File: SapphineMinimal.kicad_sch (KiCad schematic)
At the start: 0 parts

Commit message: Completed board Rev 1
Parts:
- added FID101, FID102, FID103: Fiducial, Fiducial:Fiducial_0.75mm_Mask2.25mm, symbol Mechanical:Fiducial
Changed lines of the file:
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@@
     (effects (font (size 1.27 1.27)) (justify left bottom))
+  )
+  (symbol (lib_id "Mechanical:Fiducial") (at 255.27 34.29 0) (unit 1)
+    (in_bom yes) (on_board yes) (fields_autoplaced)
+    (property "Reference" "FID102" (id 0) (at 257.429 33.4553 0)
+      (effects (font (size 1.27 1.27)) (justify left))
+    )
+    (property "Value" "Fiducial" (id 1) (at 257.429 35.9922 0)
+      (effects (font (size 1.27 1.27)) (justify left))
+    )
+    (property "Footprint" "Fiducial:Fiducial_0.75mm_Mask2.25mm" (id 2) (at 255.27 34.29 0)
+      (effects (font (size 1.27 1.27)) hide)
+    )
+    (property "Datasheet" "~" (id 3) (at 255.27 34.29 0)
+      (effects (font (size 1.27 1.27)) hide)
+    )
+  )
+  (symbol (lib_id "Mechanical:Fiducial") (at 255.27 25.4 0) (unit 1)
+    (in_bom yes) (on_board yes) (fields_autoplaced)
+    (property "Reference" "FID101" (id 0) (at 257.429 24.5653 0)
+      (effects (font (size 1.27 1.27)) (justify left))
+    )
+    (property "Value" "Fiducial" (id 1) (at 257.429 27.1022 0)
+      (effects (font (size 1.27 1.27)) (justify left))
+    )
+    (property "Footprint" "Fiducial:Fiducial_0.75mm_Mask2.25mm" (id 2) (at 255.27 25.4 0)
+      (effects (font (size 1.27 1.27)) hide)
+    )
+    (property "Datasheet" "~" (id 3) (at 255.27 25.4 0)
+      (effects (font (size 1.27 1.27)) hide)
+    )
+  )
+  (symbol (lib_id "Mechanical:Fiducial") (at 255.27 43.18 0) (unit 1)
+    (in_bom yes) (on_board yes) (fields_autoplaced)
+    (property "Reference" "FID103" (id 0) (at 257.429 42.3453 0)
+      (effects (font (size 1.27 1.27)) (justify left))
+    )
+    (property "Value" "Fiducial" (id 1) (at 257.429 44.8822 0)
+      (effects (font (size 1.27 1.27)) (justify left))
+    )
+    (property "Footprint" "Fiducial:Fiducial_0.75mm_Mask2.25mm" (id 2) (at 255.27 43.18 0)
+      (effects (font (size 1.27 1.27)) hide)
+    )
+    (property "Datasheet" "~" (id 3) (at 255.27 43.18 0)
+      (effects (font (size 1.27 1.27)) hide)
+    )
   )
   (sheet (at 181.61 46.99) (size 38.1 27.94) (fields_autoplaced)
@@
       (reference "FB801") (unit 1) (value "FerriteBead") (footprint "Inductor_SMD:L_0201_0603Metric")
     )
+    (path "/425001ac-1f75-42e4-b850-928c7a40b141"
+      (reference "FID101") (unit 1) (value "Fiducial") (footprint "Fiducial:Fiducial_0.75mm_Mask2.25mm")
+    )
+    (path "/2acc44b4-fb4e-460d-83c5-dc8f7d66c881"
+      (reference "FID102") (unit 1) (value "Fiducial") (footprint "Fiducial:Fiducial_0.75mm_Mask2.25mm")
+    )
+    (path "/ba9cefc2-e855-411c-bf9e-6a189e250684"
+      (reference "FID103") (unit 1) (value "Fiducial") (footprint "Fiducial:Fiducial_0.75mm_Mask2.25mm")
+    )
     (path "/00000000-0000-0000-0000-00005e3fe689/00000000-0000-0000-0000-00005e66dbe9"

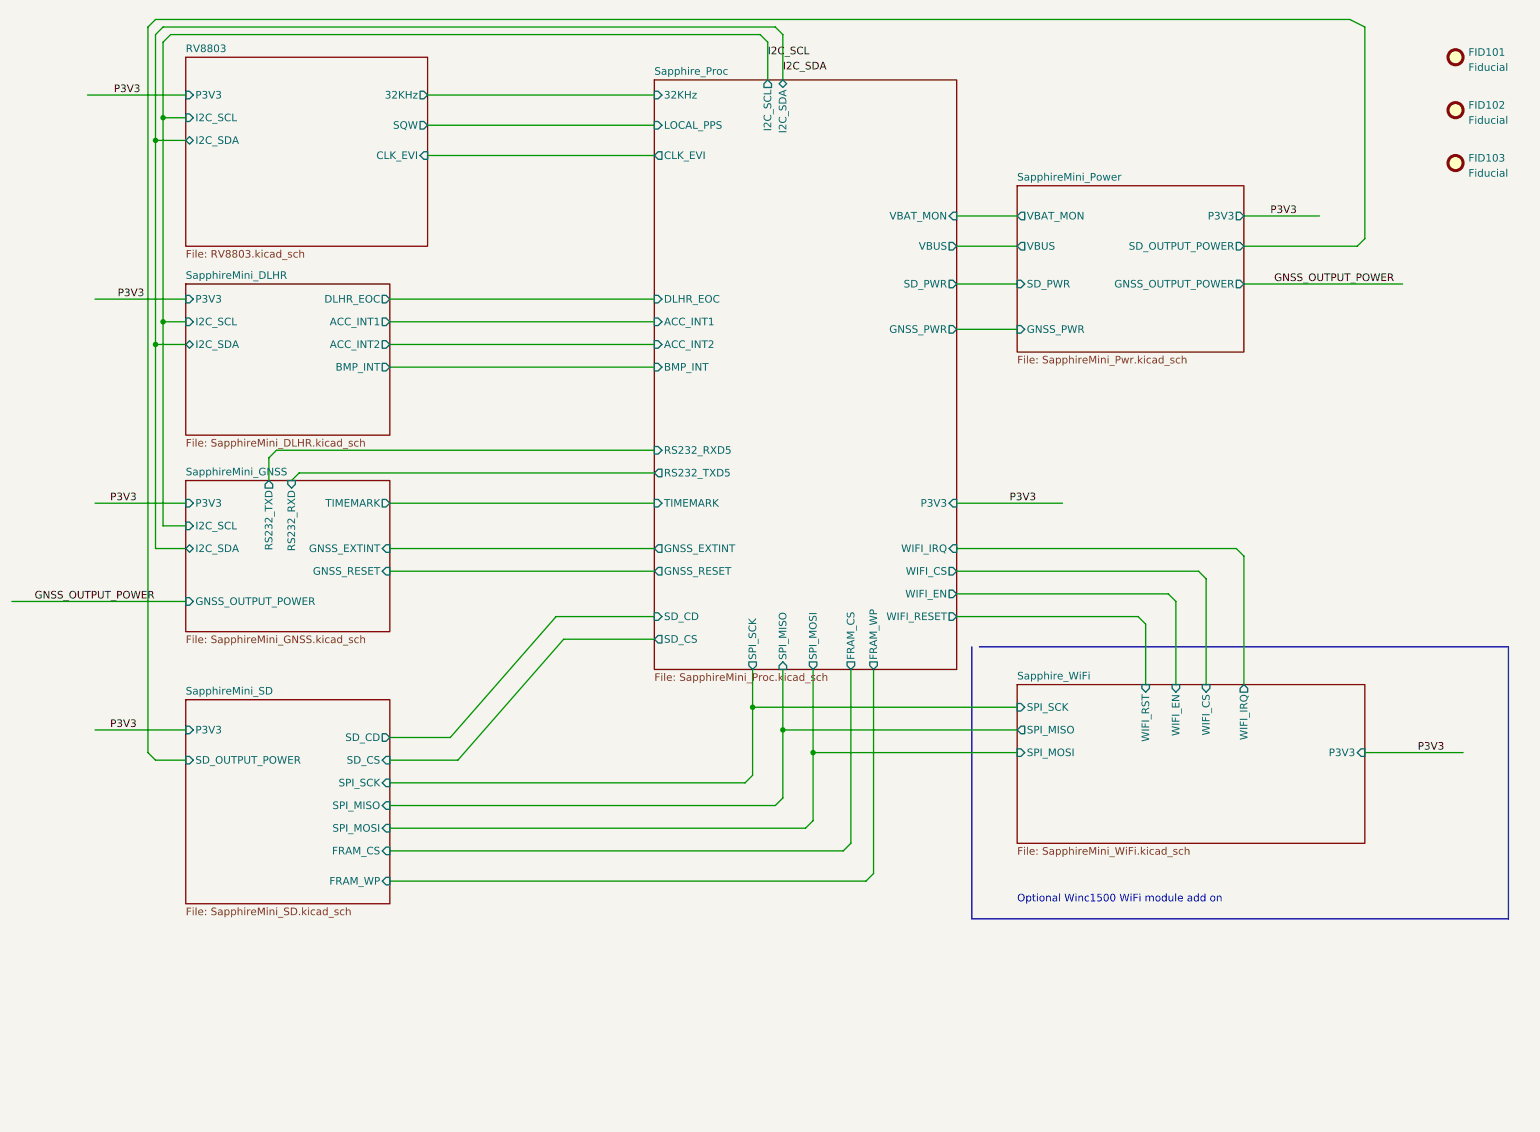
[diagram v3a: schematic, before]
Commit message: updated new layout - no routing
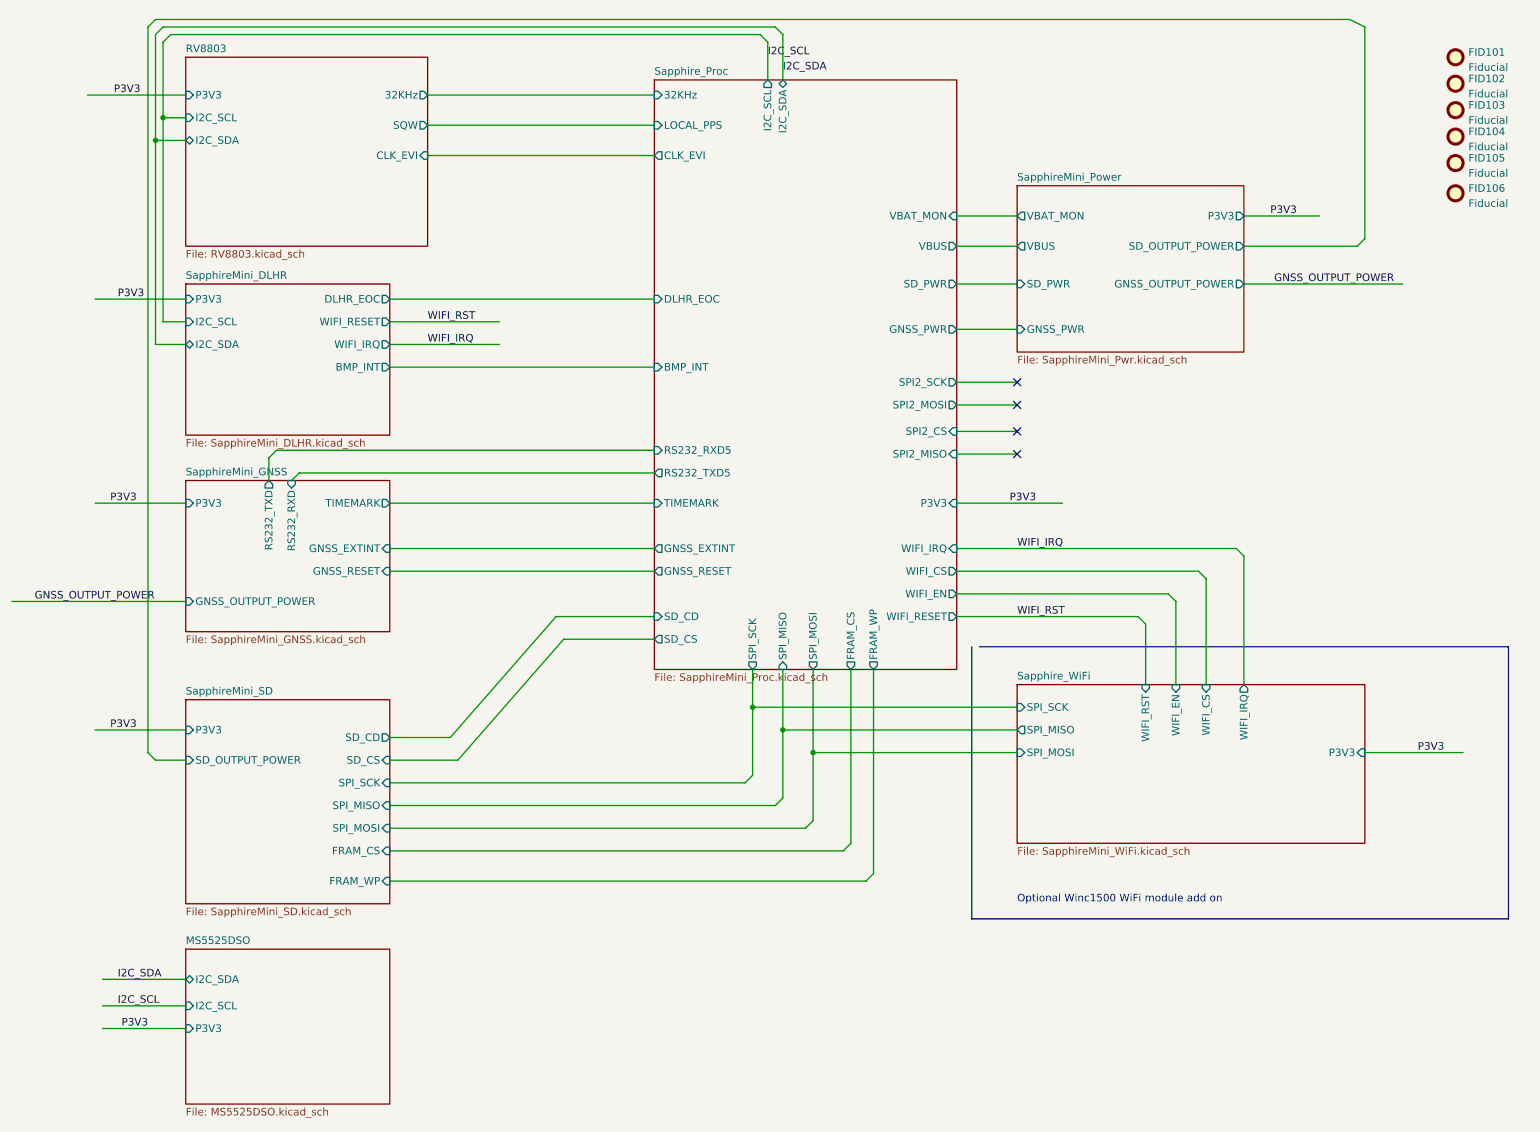
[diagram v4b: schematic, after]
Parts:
- added FID104, FID105, FID106: Fiducial, Fiducial:Fiducial_0.5mm_Mask1mm, symbol Mechanical:Fiducial
- FID101, FID102, FID103: footprint Fiducial:Fiducial_0.75mm_Mask2.25mm -> Fiducial:Fiducial_0.5mm_Mask1mm
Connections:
- no-connect marks 0 -> 4
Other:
- added sheet MS5525DSO (MS5525DSO.kicad_sch)
- sheet SapphireMini_DLHR ports: added WIFI_IRQ, WIFI_RESET; removed ACC_INT1, ACC_INT2
- sheet SapphireMini_GNSS ports: added none; removed I2C_SCL, I2C_SDA
- sheet Sapphire_Proc ports: added SPI2_CS, SPI2_MISO, SPI2_MOSI, SPI2_SCK; removed ACC_INT1, ACC_INT2

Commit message: 6 Layer Routing
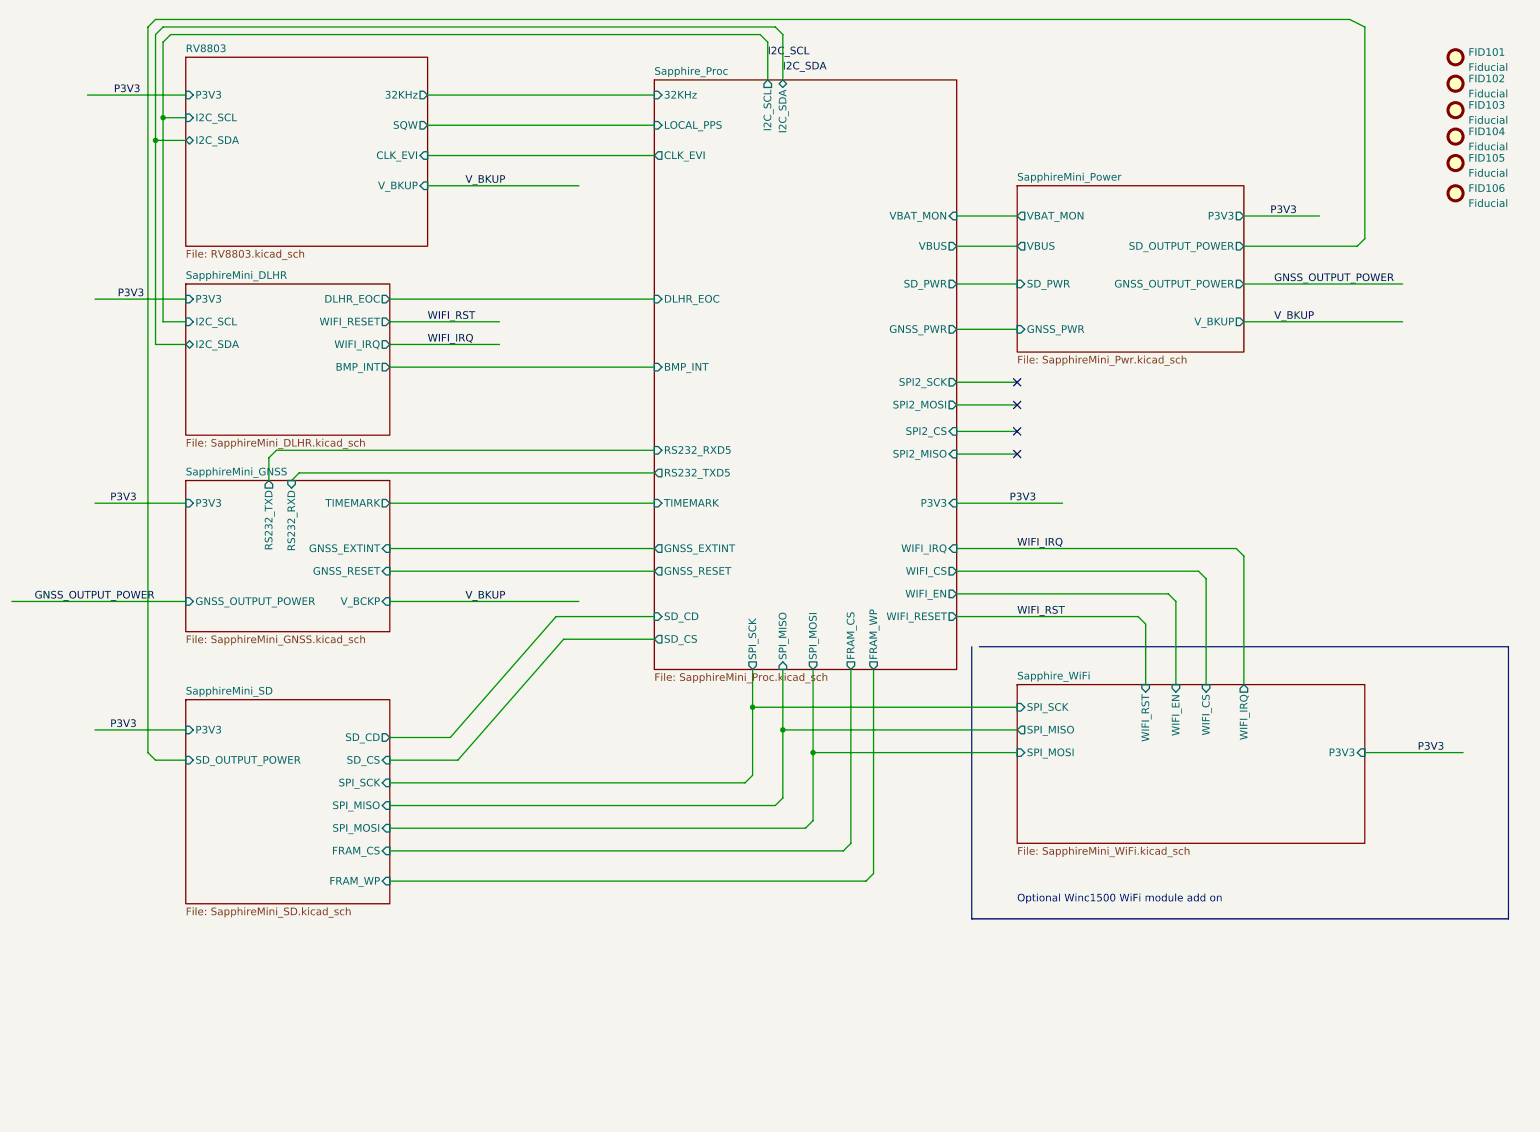
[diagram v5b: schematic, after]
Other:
- removed sheet MS5525DSO
- sheet RV8803 ports: added V_BKUP; removed none
- sheet SapphireMini_GNSS ports: added V_BCKP; removed none
- sheet SapphireMini_Power ports: added V_BKUP; removed none

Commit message: Release to OSH Park
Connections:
- no-connect marks 4 -> 1
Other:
- sheet Sapphire_WiFi ports: added SPI2_MISO, SPI2_MOSI, SPI2_SCK; removed none
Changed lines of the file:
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@@
   (junction (at 147.32 142.24) (diameter 0) (color 0 0 0 0)
   )
-  (no_connect (at 181.61 80.01))
-  (no_connect (at 181.61 83.82))
   (no_connect (at 181.61 88.265))
-  (no_connect (at 181.61 92.075))
   (wire (pts (xy 146.05 154.94) (xy 147.32 153.67))
     (stroke (width 0) (type default) (color 0 0 0 0))
@@
     (stroke (width 0) (type default) (color 0 0 0 0))
   )
+  (wire (pts (xy 170.18 149.86) (xy 181.61 149.86))
+    (stroke (width 0) (type default) (color 0 0 0 0))
+  )
   (wire (pts (xy 171.45 107.95) (xy 218.44 107.95))
     (stroke (width 0) (type default) (color 0 0 0 0))
@@
     (stroke (width 0) (type default) (color 0 0 0 0))
   )
+  (wire (pts (xy 170.18 153.67) (xy 181.61 153.67))
+    (stroke (width 0) (type default) (color 0 0 0 0))
+  )
   (wire (pts (xy 55.88 96.52) (xy 55.88 92.71))
     (stroke (width 0) (type default) (color 0 0 0 0))
@@
     (stroke (width 0) (type default) (color 0 0 0 0))
   )
+  (wire (pts (xy 170.18 146.05) (xy 181.61 146.05))
+    (stroke (width 0) (type default) (color 0 0 0 0))
+  )
   (wire (pts (xy 171.45 52.07) (xy 181.61 52.07))
     (stroke (width 0) (type default) (color 0 0 0 0))
@@
     (effects (font (size 1.27 1.27)) (justify left bottom))
   )
+  (label "SPI2_SCK" (at 172.72 80.01 0)
+    (effects (font (size 1.27 1.27)) (justify left bottom))
+  )
   (label "WIFI_IRQ" (at 181.61 107.95 0)
     (effects (font (size 1.27 1.27)) (justify left bottom))
@@
     (effects (font (size 1.27 1.27)) (justify left bottom))
   )
+  (label "SPI2_MISO" (at 172.72 92.075 0)
+    (effects (font (size 1.27 1.27)) (justify left bottom))
+  )
+  (label "SPI2_MISO" (at 171.45 149.86 0)
+    (effects (font (size 1.27 1.27)) (justify left bottom))
+  )
   (label "I2C_SDA" (at 142.24 27.94 0)
     (effects (font (size 1.27 1.27)) (justify left bottom))
@@
   )
   (label "P3V3" (at 30.48 66.04 0)
+    (effects (font (size 1.27 1.27)) (justify left bottom))
+  )
+  (label "SPI2_MOSI" (at 171.45 153.67 0)
     (effects (font (size 1.27 1.27)) (justify left bottom))
   )
@@
     (effects (font (size 1.27 1.27)) (justify left bottom))
   )
+  (label "SPI2_SCK" (at 171.45 146.05 0)
+    (effects (font (size 1.27 1.27)) (justify left bottom))
+  )
   (label "P3V3" (at 180.34 100.33 0)
     (effects (font (size 1.27 1.27)) (justify left bottom))
@@
   (label "P3V3" (at 228.6 52.07 180)
     (effects (font (size 1.27 1.27)) (justify right bottom))
+  )
+  (label "SPI2_MOSI" (at 172.72 83.82 0)
+    (effects (font (size 1.27 1.27)) (justify left bottom))
   )
   (label "P3V3" (at 29.21 100.33 0)
@@
     (pin "P3V3" input (at 240.03 142.24 0)
       (effects (font (size 1.27 1.27)) (justify right))
+    )
+    (pin "SPI2_MISO" output (at 181.61 149.86 180)
+      (effects (font (size 1.27 1.27)) (justify left))
+    )
+    (pin "SPI2_SCK" input (at 181.61 146.05 180)
+      (effects (font (size 1.27 1.27)) (justify left))
+    )
+    (pin "SPI2_MOSI" input (at 181.61 153.67 180)
+      (effects (font (size 1.27 1.27)) (justify left))
     )
   )
@@
       (reference "R515") (unit 1) (value "20K0") (footprint "Resistor_SMD:R_0603_1608Metric")
     )
+    (path "/00000000-0000-0000-0000-000063a74ef2/80569536-1248-42b2-916b-4673ea3b3e96"
+      (reference "R601") (unit 1) (value "0") (footprint "Resistor_SMD:R_0603_1608Metric")
+    )
+    (path "/00000000-0000-0000-0000-000063a74ef2/770a810f-7184-4b44-9425-19097f9992b5"
+      (reference "R602") (unit 1) (value "0") (footprint "Resistor_SMD:R_0603_1608Metric")
+    )
+    (path "/00000000-0000-0000-0000-000063a74ef2/c26ca922-835a-4202-97d2-3b260d7d3c1c"
+      (reference "R603") (unit 1) (value "47") (footprint "Resistor_SMD:R_0603_1608Metric")
+    )
+    (path "/00000000-0000-0000-0000-000063a74ef2/1ac05411-172f-4596-b704-63622c2c6dfa"
+      (reference "R604") (unit 1) (value "47") (footprint "Resistor_SMD:R_0603_1608Metric")
+    )
     (path "/00000000-0000-0000-0000-000063a74ef2/6d43920e-21c5-441e-8415-c5dfb7b75379"
